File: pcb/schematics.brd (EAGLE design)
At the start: 74.6 x 80 mm, 8 parts, among them IC1 MEGA8-P, X1 22-23-2051, X2 22-23-2051

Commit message: Update eagle files
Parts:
- added C1: (no value), rcl:C025-025X050
- moved BTNR 25.1 mm to (9.62, 43.2)
- moved SOIL 17.0 mm to (36.8, 24.1)
- moved U$1 13.3 mm to (24.1, 40.1)
- moved U$2 12.0 mm to (7.62, 17.2)
- moved X1 12.0 mm to (40.6, 5.78)
- moved BTN 10.0 mm to (8.62, 51.1)
- moved IC1 8.00 mm to (24.1, 37.7)
- moved X2 8.00 mm to (24.1, 14.1)
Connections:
- removed net N$3: BTNR.2, IC1.22, IC1.8, SOIL.2, U$1.1, U$2.1, X1.1, X2.1
- new net GND: BTNR.2, C1.2, IC1.22, IC1.8, SOIL.2, U$1.1, U$2.1, X1.1, X2.1
- net N$5: now also C1.1
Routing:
- net N$3: track 114.6 -> 0.00 mm
- net GND: track 0.00 -> 46.1 mm
- net N$5: track 216.5 -> 188.5 mm
- net N$4: track 32.5 -> 47.2 mm
- net N$2: track 80.0 -> 70.0 mm
- net N$7: track 5.13 -> 12.8 mm
- net N$6: track 16.4 -> 9.03 mm
- net N$1: track 81.3 -> 75.6 mm
- net N$9: track 21.2 -> 26.1 mm
- net N$8: track 19.6 -> 15.9 mm
- added copper zone on layer 16, net GND
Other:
- board size 74.6 x 80 mm -> 57.6 x 64 mm
- board text added: "SOIL MOISTURE MONITOR"

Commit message: Update eagle files
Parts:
- moved IC1 4.47 mm to (22.1, 33.7)
- moved U$1 4.47 mm to (22.1, 36.1)
- moved BTNR 4.47 mm to (7.62, 39.2)
- moved SOIL 4.24 mm to (33.8, 21.1)
- moved X1 4.24 mm to (37.6, 2.78)
- moved BTN 4.12 mm to (7.62, 47.1)
- moved C1 3.61 mm to (8.00, 36.0)
- moved X2 3.61 mm to (22.1, 11.1)
- moved U$2 3.16 mm to (6.62, 14.2)
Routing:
- net N$2: track 70.0 -> 67.7 mm
- net N$5: track 188.5 -> 186.5 mm
- net N$4: track 47.2 -> 45.4 mm
- net N$1: track 75.6 -> 74.2 mm
- net N$8: track 15.9 -> 14.9 mm
- net N$9: track 26.1 -> 25.2 mm
- net GND: track 46.1 -> 46.7 mm
- net N$6: track 9.03 -> 8.45 mm
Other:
- board size 57.6 x 64 mm -> 54.6 x 63 mm

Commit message: Update eagle files
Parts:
- moved C1 1.00 mm to (9.00, 36.0)
- moved BTN 1.00 mm to (8.62, 47.1)
- moved BTNR 1.00 mm to (8.62, 39.2)
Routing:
- net N$9: track 25.2 -> 31.7 mm
- net N$2: track 67.7 -> 73.7 mm
- net N$5: track 186.5 -> 182.9 mm
- net N$8: track 14.9 -> 13.9 mm
- net N$7: track 13.2 -> 12.4 mm
- net GND: track 46.7 -> 45.9 mm
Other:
- board size 54.6 x 63 mm -> 53.6 x 63 mm

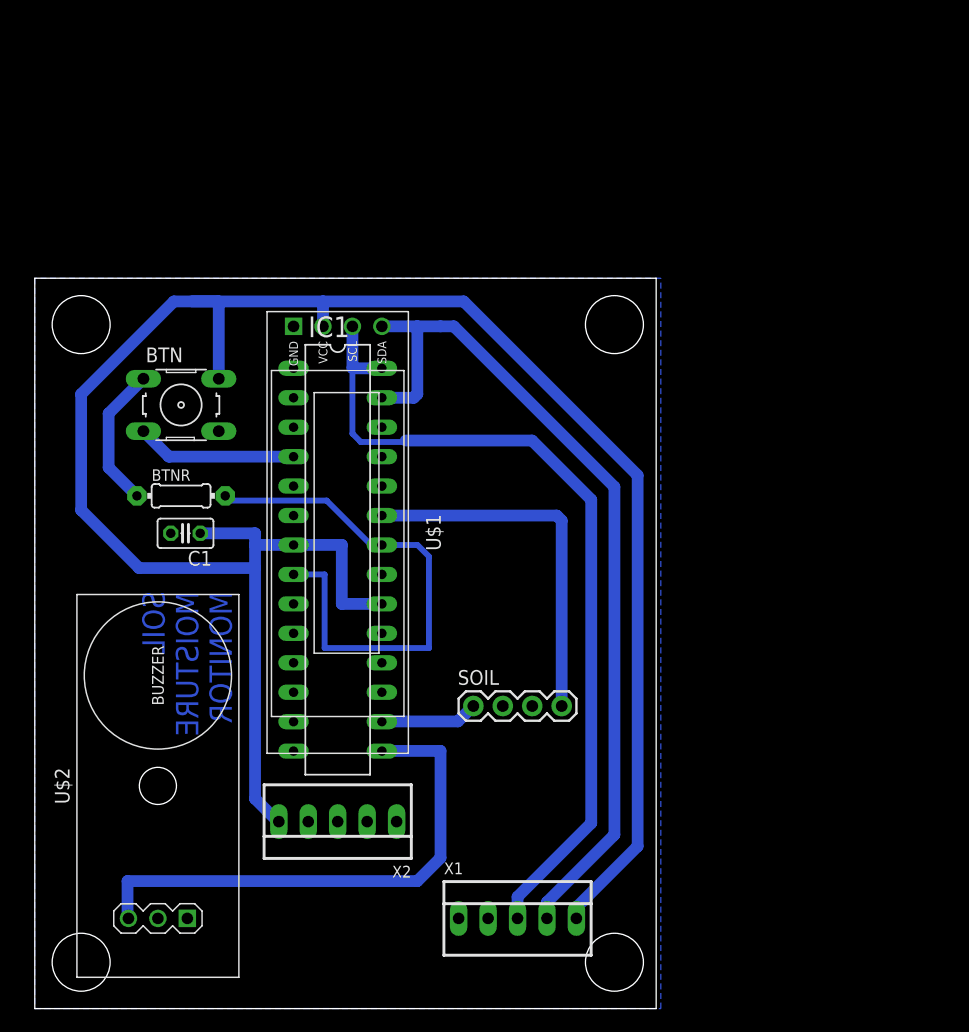
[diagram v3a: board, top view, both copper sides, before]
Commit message: Update eagle files (shrinking the board)
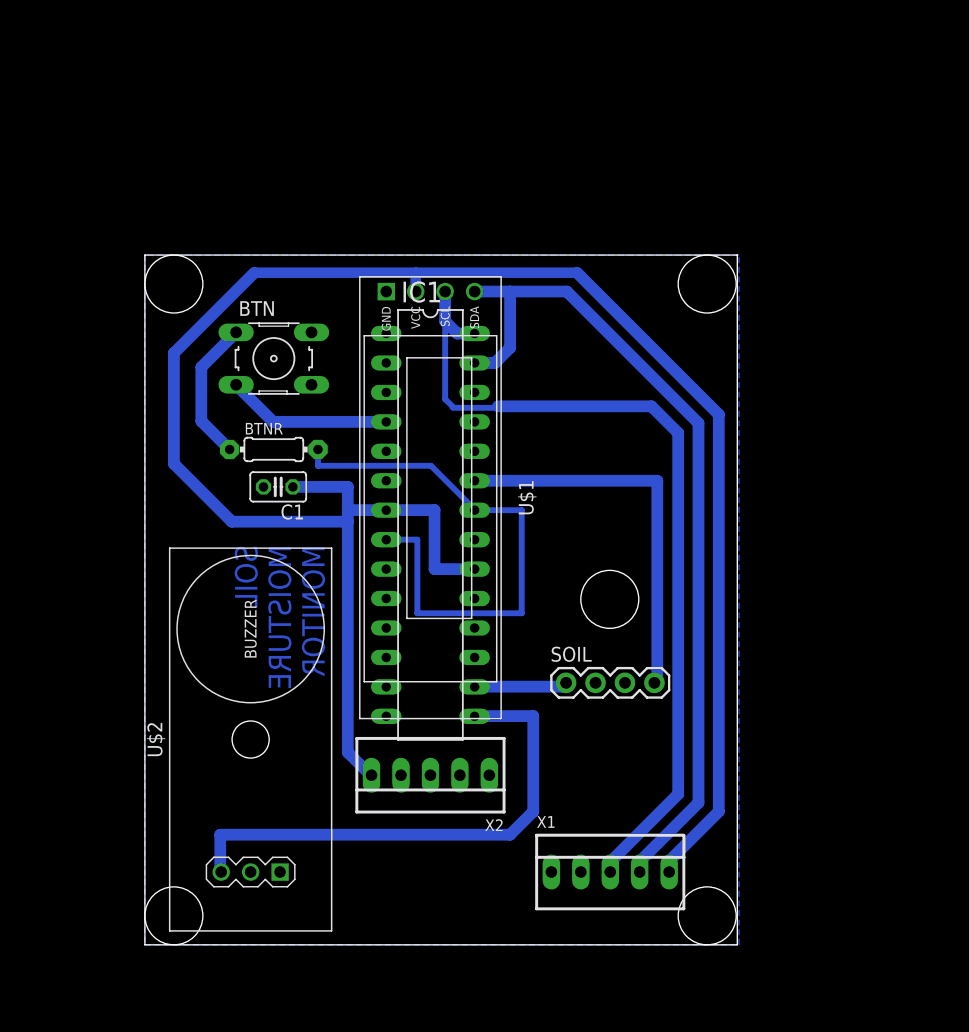
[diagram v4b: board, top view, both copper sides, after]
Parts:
- moved BTN 8.94 mm to (16.6, 51.1)
- moved BTNR 8.94 mm to (16.6, 43.2)
- moved C1 8.94 mm to (17.0, 40.0)
- moved X1 8.94 mm to (45.6, 6.78)
- moved X2 8.94 mm to (30.1, 15.1)
- moved U$2 8.94 mm to (14.6, 18.2)
- moved IC1 8.54 mm to (30.1, 36.7)
- moved U$1 8.54 mm to (30.1, 39.1)
- moved SOIL 8.25 mm to (41.8, 23.1)
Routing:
- net N$5: track 182.9 -> 171.0 mm
- net N$2: track 73.7 -> 75.8 mm
- net GND: track 45.9 -> 47.5 mm
- net N$9: track 31.7 -> 33.3 mm
- net N$1: track 74.5 -> 73.3 mm
- net N$4: track 45.4 -> 44.4 mm
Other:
- board size 53.6 x 63 mm -> 51.1 x 59.5 mm

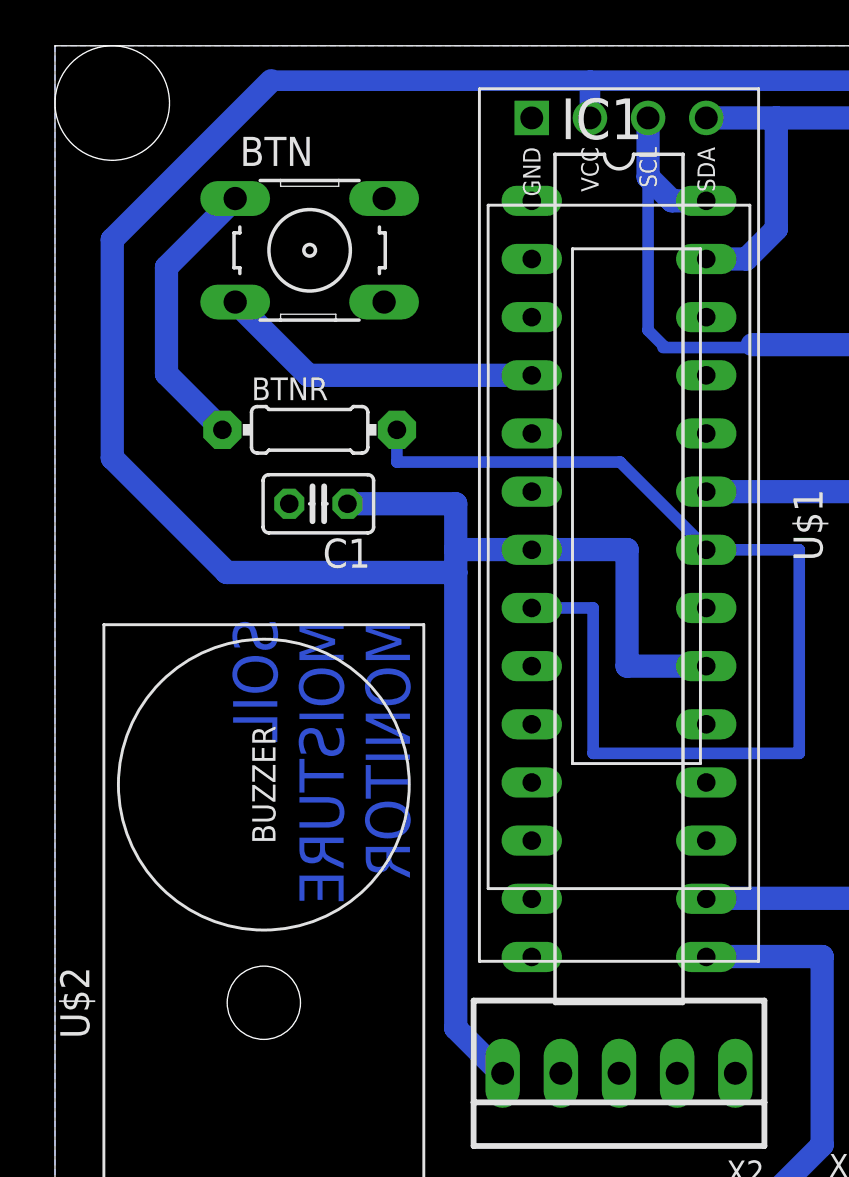
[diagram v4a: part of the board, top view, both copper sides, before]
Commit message: Add slide switch
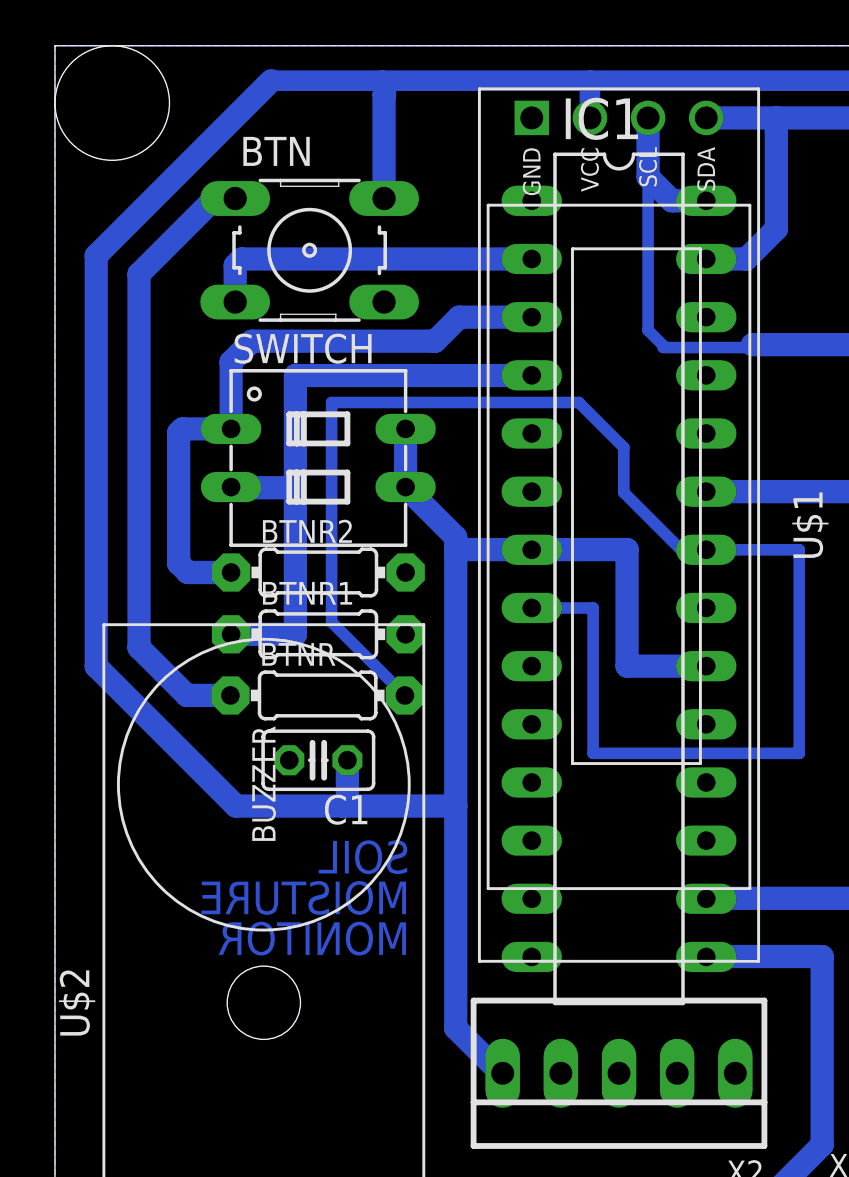
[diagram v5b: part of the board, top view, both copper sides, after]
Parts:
- added BTNR1, BTNR2: (no value), adafruit:0204/7
- added SWITCH: (no value), switch-dil:DIP02YL
- moved BTNR 11.6 mm to (17.0, 31.6)
- moved C1 11.2 mm to (17.0, 28.8)
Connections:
- new net N$10: BTNR1.1, IC1.4, SWITCH.2
- new net N$3: BTNR2.1, IC1.3, SWITCH.1
- net GND: now also BTNR1.2, BTNR2.2
- net N$5: now also SWITCH.3, SWITCH.4
- net N$8: now also IC1.2; no longer IC1.4
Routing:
- net N$3: track 0.00 -> 27.4 mm
- net N$10: track 0.00 -> 27.3 mm
- net GND: track 47.5 -> 65.3 mm
- net N$5: track 171.0 -> 188.3 mm
- net N$7: track 12.4 -> 26.7 mm

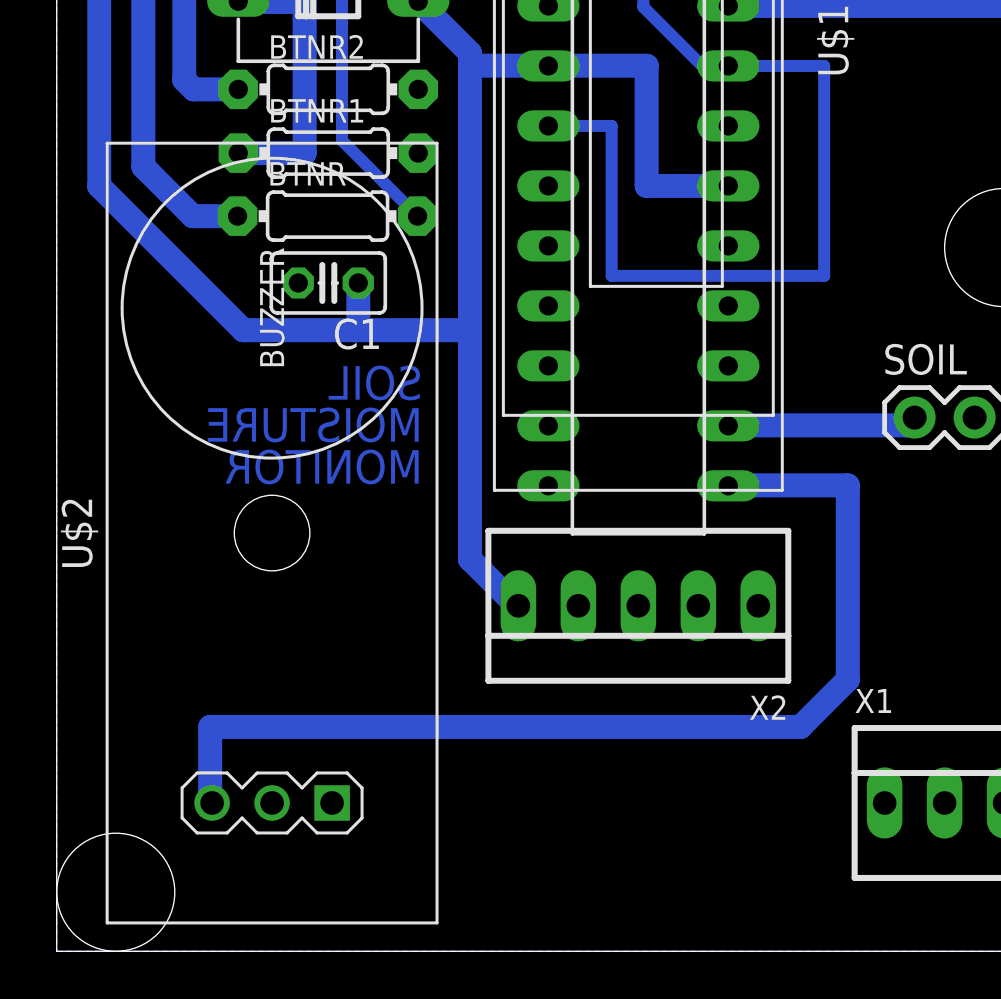
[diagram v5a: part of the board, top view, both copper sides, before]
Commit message: Upadate pcb to use passive buzzer
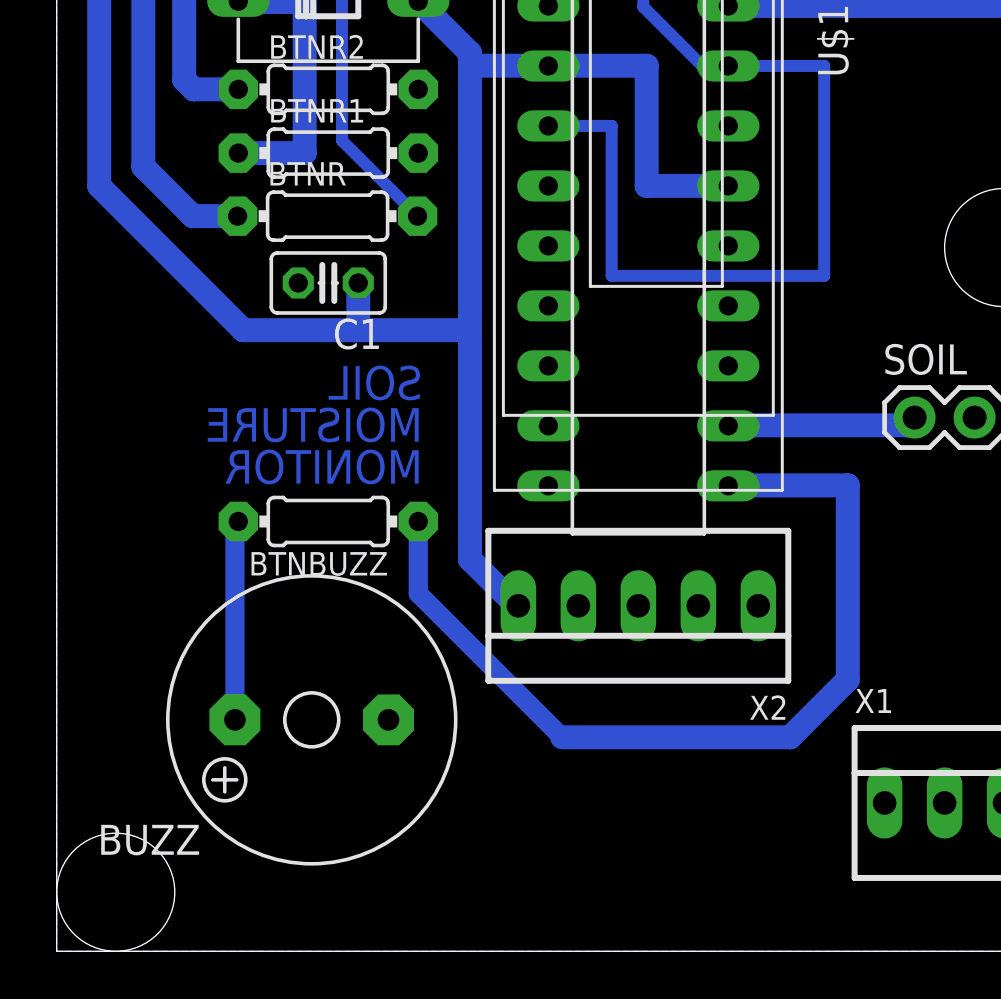
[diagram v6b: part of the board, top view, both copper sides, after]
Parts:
- removed U$2: SOUND-BUZZER, diy-modules:SOUND-BUZZER
- added BTNBUZZ: (no value), adafruit:0204/7
- added BUZZ: F/QMX, buzzer:F/QMX
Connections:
- new net N$11: BTNBUZZ.2, BUZZ.+
- net GND: now also BUZZ.-; no longer U$2.1
- net N$4: now also BTNBUZZ.1; no longer U$2.3
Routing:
- net N$11: track 0.00 -> 8.46 mm
- net N$4: track 44.4 -> 38.1 mm
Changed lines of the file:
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@@
 <attribute name="VALUE" x="22.51" y="39.07" size="1.27" layer="27" rot="R270" align="top-center"/>
-</element>
-<element name="U$2" library="diy-modules" package="SOUND-BUZZER" value="SOUND-BUZZER" x="14.62" y="18.21" smashed="yes" rot="R90">
-<attribute name="NAME" x="7" y="18.21" size="1.27" layer="25" rot="R90" align="bottom-center"/>
-<attribute name="VALUE" x="22.24" y="18.21" size="1.27" layer="27" rot="R90" align="top-center"/>
 </element>
 <element name="SOIL" library="adafruit" library_urn="urn:adsk.eagle:library:420" package="1X04-BIG" package3d_urn="urn:adsk.eagle:package:6240658/1" value="1X4-BIG" x="41.83" y="23.1" smashed="yes">
@@
 <attribute name="NAME" x="14.46" y="38.2954" size="0.9906" layer="25" ratio="12"/>
 <attribute name="VALUE" x="15.3744" y="36.5174" size="0.9906" layer="27" ratio="12"/>
+</element>
+<element name="BUZZ" library="buzzer" library_urn="urn:adsk.eagle:library:113" package="F/QMX" package3d_urn="urn:adsk.eagle:package:5278/1" value="F/QMX" x="16.3" y="10.3" smashed="yes" rot="R180">
+<attribute name="MF" value="" x="16.3" y="10.3" size="1.778" layer="27" rot="R180" display="off"/>
+<attribute name="MPN" value="" x="16.3" y="10.3" size="1.778" layer="27" rot="R180" display="off"/>
+<attribute name="NAME" x="11.601" y="5.855" size="1.27" layer="25" ratio="10" rot="R180"/>
+<attribute name="OC_FARNELL" value="unknown" x="16.3" y="10.3" size="1.778" layer="27" rot="R180" display="off"/>
+<attribute name="OC_NEWARK" value="unknown" x="16.3" y="10.3" size="1.778" layer="27" rot="R180" display="off"/>
+<attribute name="POPULARITY" value="4" x="16.3" y="10.3" size="1.778" layer="27" rot="R180" display="off"/>
+<attribute name="VALUE" x="19.856" y="14.11" size="1.27" layer="27" ratio="10" rot="R180"/>
+</element>
+<element name="BTNBUZZ" library="adafruit" library_urn="urn:adsk.eagle:library:420" package="0204/7" package3d_urn="urn:adsk.eagle:package:6240596/1" value="" x="17" y="18.7" smashed="yes" rot="R180">
+<attribute name="NAME" x="19.54" y="17.4046" size="0.9906" layer="25" ratio="12" rot="R180"/>
+<attribute name="VALUE" x="18.6256" y="19.1826" size="0.9906" layer="27" ratio="12" rot="R180"/>
 </element>
 </elements>
@@
 </signal>
 <signal name="GND">
-<contactref element="U$2" pad="1"/>
 <contactref element="IC1" pad="8"/>
 <contactref element="U$1" pad="1"/>
@@
 <contactref element="BTNR2" pad="2"/>
 <contactref element="BTNR1" pad="2"/>
+<contactref element="BUZZ" pad="-"/>
 </signal>
 <signal name="N$4">
 <contactref element="IC1" pad="15"/>
-<contactref element="U$2" pad="3"/>
 <wire x1="39" y1="20.2286" x2="33.9586" y2="20.2286" width="1.016" layer="16"/>
 <wire x1="33.94" y1="20.21" x2="33.9586" y2="20.2286" width="1.016" layer="16"/>
 <wire x1="39" y1="20.2286" x2="39" y2="12" width="1.016" layer="16"/>
-<wire x1="39" y1="12" x2="37" y2="10" width="1.016" layer="16"/>
-<wire x1="12" y1="10" x2="12" y2="6.86" width="1.016" layer="16"/>
-<wire x1="12" y1="6.86" x2="12.08" y2="6.78" width="1.016" layer="16"/>
-<wire x1="37" y1="10" x2="12" y2="10" width="1.016" layer="16"/>
+<wire x1="39" y1="12" x2="36.56" y2="9.56" width="1.016" layer="16"/>
+<wire x1="26.9" y1="9.56" x2="36.56" y2="9.56" width="1.016" layer="16"/>
+<contactref element="BTNBUZZ" pad="1"/>
+<wire x1="20.81" y1="18.7" x2="20.81" y2="15.65" width="0.8128" layer="16"/>
+<wire x1="20.81" y1="15.65" x2="26.9" y2="9.56" width="0.8128" layer="16"/>
 </signal>
 <signal name="N$5">
@@
 <wire x1="16" y1="34.3" x2="13.19" y2="34.3" width="1.016" layer="16"/>
 </signal>
+<signal name="N$11">
+<contactref element="BUZZ" pad="+"/>
+<contactref element="BTNBUZZ" pad="2"/>
+<wire x1="13.0488" y1="10.3" x2="13.0488" y2="18.5588" width="0.8128" layer="16"/>
+<wire x1="13.0488" y1="18.5588" x2="13.19" y2="18.7" width="0.8128" layer="16"/>
+</signal>
 </signals>
